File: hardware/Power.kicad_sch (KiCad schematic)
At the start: 5 parts, among them J3 USB_C_Receptacle_USB2.0_16P, U5 USBLC6-2SC6Y

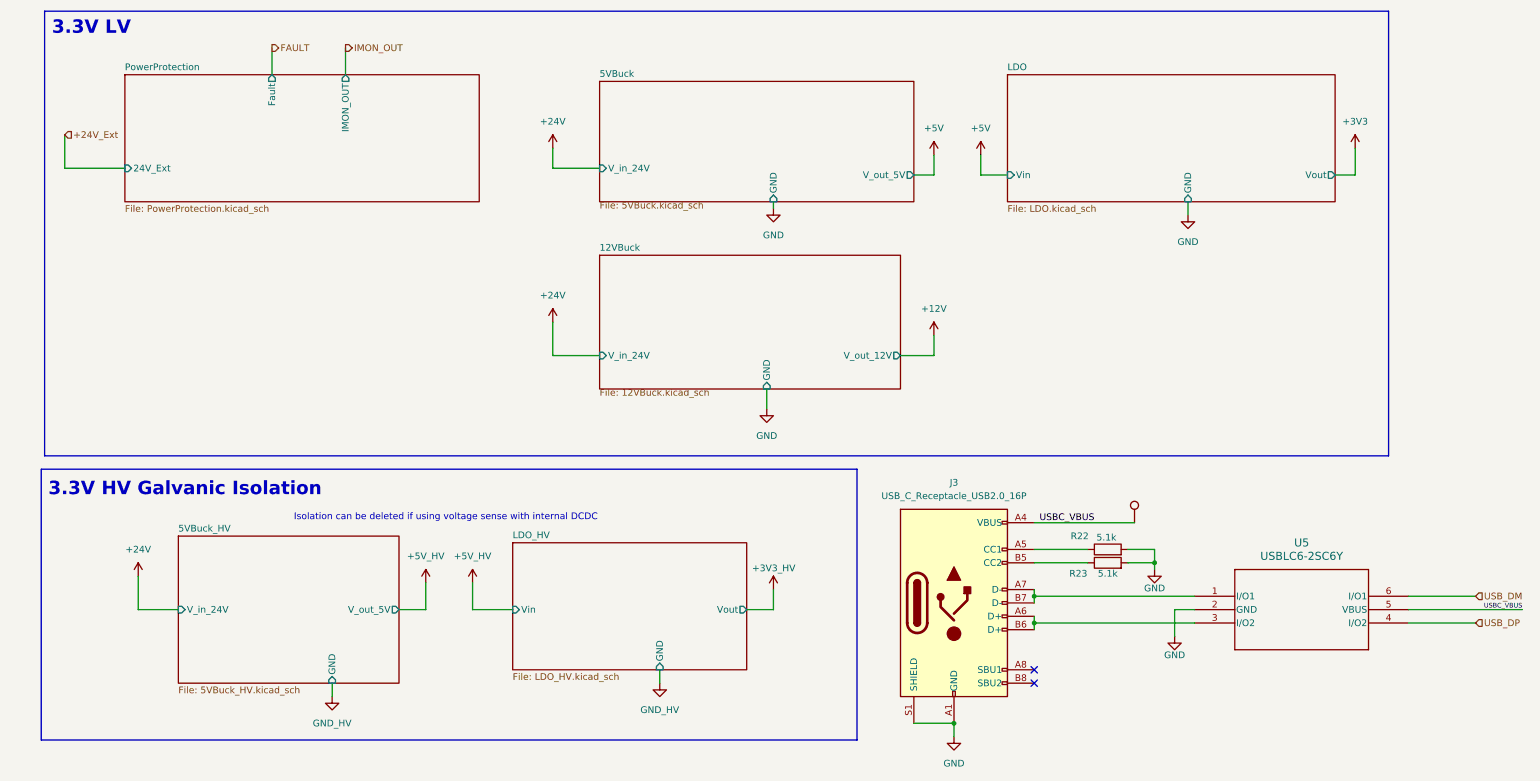
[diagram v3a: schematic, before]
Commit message: addressed 75% of review council 2, cleaned up ERC errors, embedded datasheet and PN
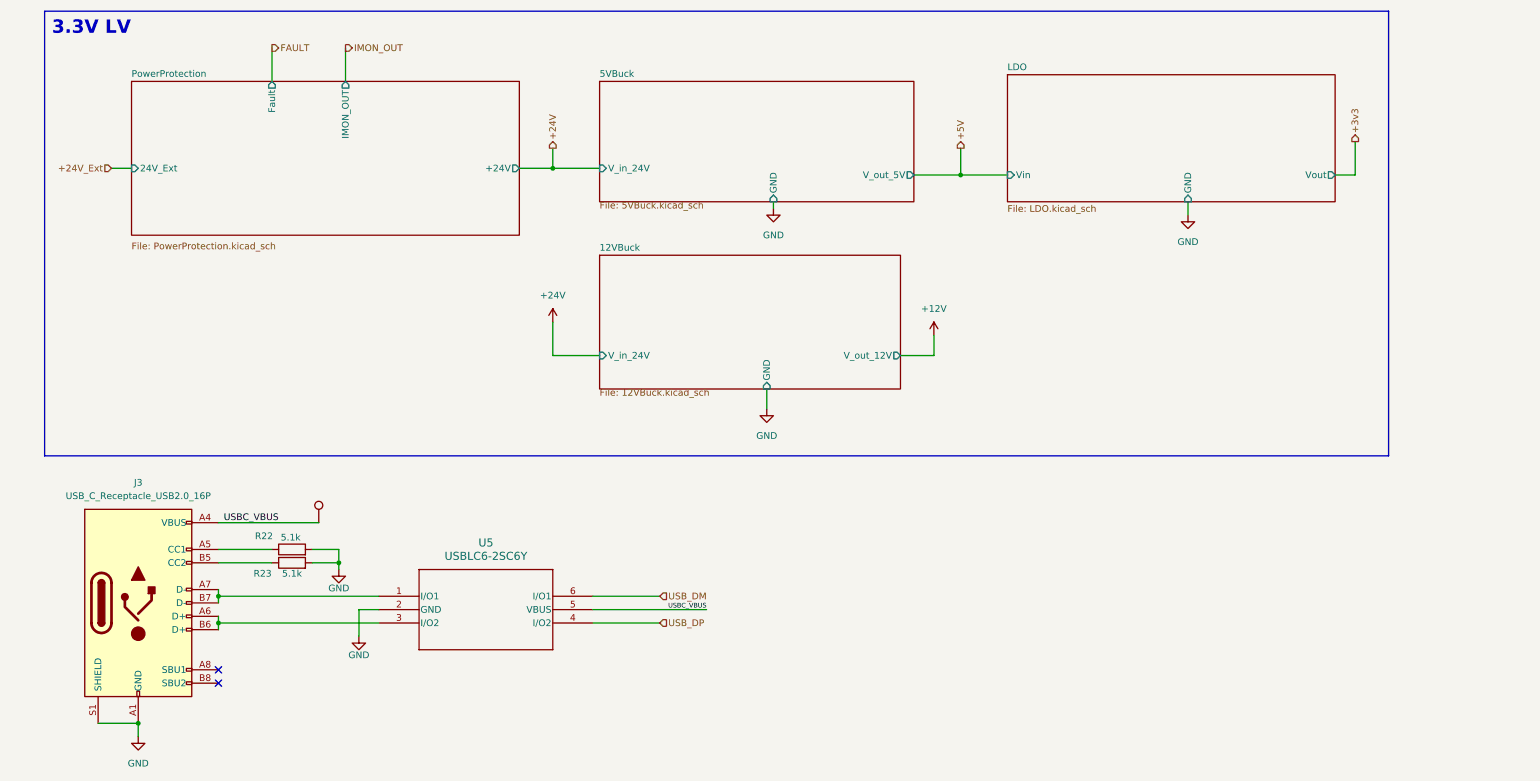
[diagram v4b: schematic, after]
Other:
- removed sheet 5VBuck_HV
- removed sheet LDO_HV
- sheet PowerProtection ports: added +24V; removed none
- note removed: "3.3V HV Galvanic Isolation"
- note removed: "Isolation can be deleted if using voltage sense with internal DCDC"
- moved on the sheet: J3, R22, R23, U5

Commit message: added calcs, cleaned up, addressed comments
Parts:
- added TP12: PP GATE, symbol Connector:TestPoint
- added TP13: PP EN, symbol Connector:TestPoint
- added TP14: PP OV, symbol Connector:TestPoint
- added TP15: PP SOURCE, symbol Connector:TestPoint
- renumbered J3 to J7, R22 to R27, R23 to R28, TP19 to TP11, U5 to U4
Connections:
- new net PowerProtection/EN/UVLO: TP13.1
- new net PowerProtection/OV: TP14.1
- new net PowerProtection/gate: TP12.1
- new net PowerProtection/source: TP15.1
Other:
- removed sheet 12VBuck
- sheet PowerProtection ports: added EN/UVLO, GND, OV, Vin, Vout, gate, source; removed +24V, 24V_Ext, Fault, IMON_OUT
- note added: "Power"
- note removed: "3.3V LV"
- moved on the sheet: J7, R27, R28, U4

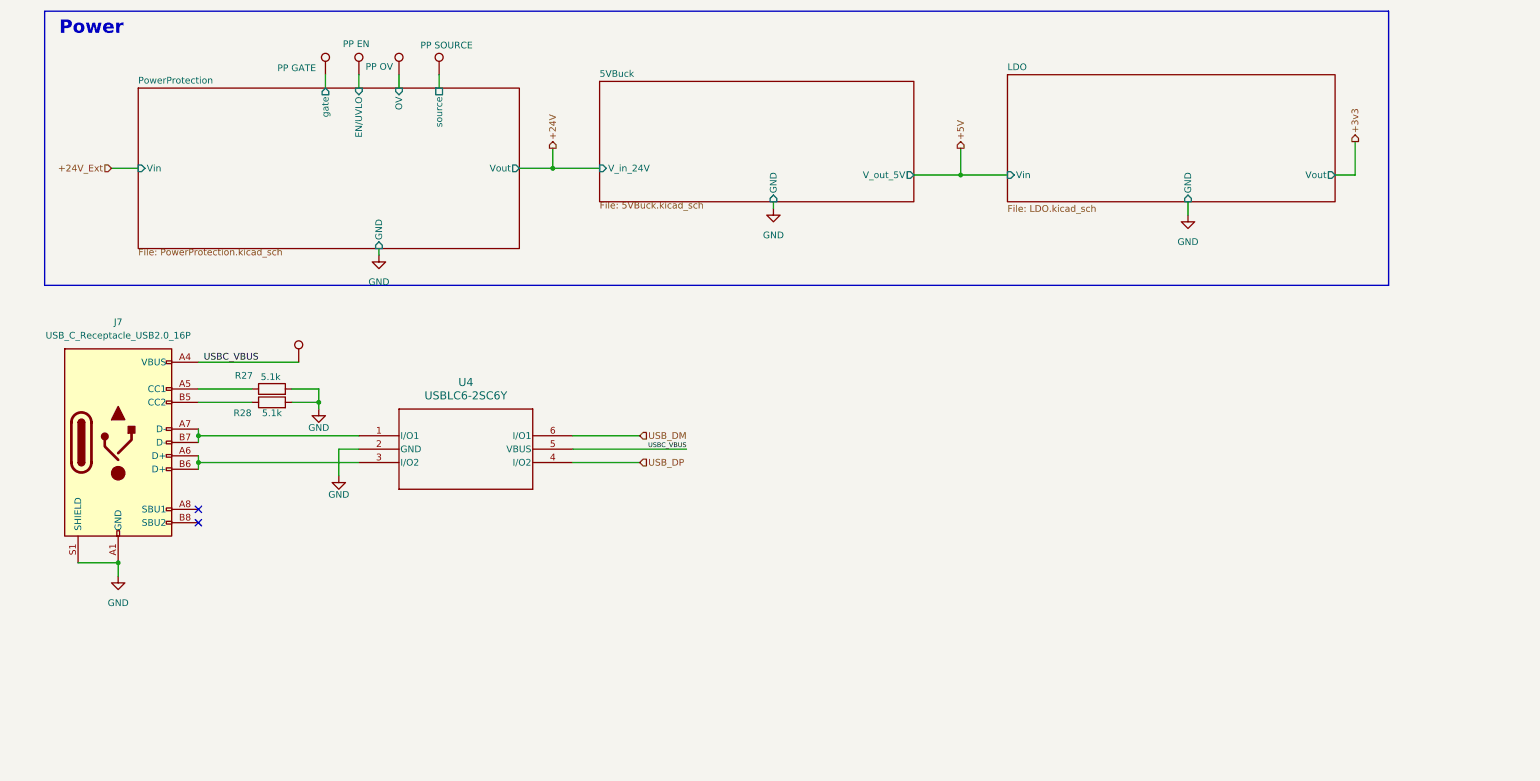
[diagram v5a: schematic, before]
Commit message: added USB power mux
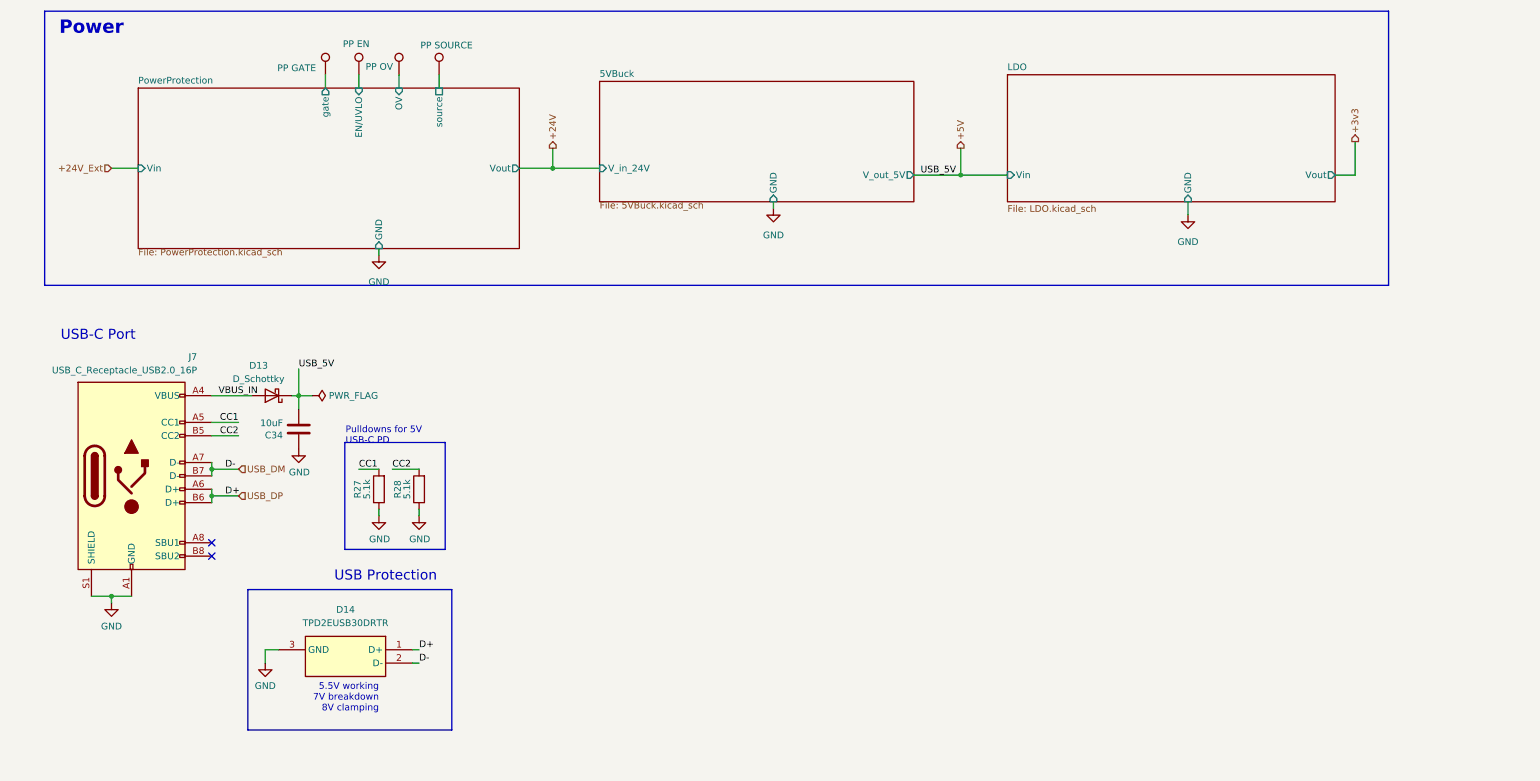
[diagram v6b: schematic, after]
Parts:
- removed J7: USB_C_Receptacle_USB2.0_16P, LHRS_ICs:USB_C_Receptacle_GCT_USB4105-xx-A_16P_TopMnt_Horizontal, symbol lhrs_connectors:USB_C_Receptacle_USB2.0_16P
- removed TP11: TestPoint, symbol Connector:TestPoint
- removed U4: USBLC6-2SC6Y, SOT23-6L_STM, symbol USBLC6_2SC6Y:USBLC6-2SC6Y
- added C34: 10uF, Capacitor_SMD:C_0805_2012Metric, symbol Device:C
- added D13: D_Schottky, Diode_SMD:D_SOD-123, symbol Device:D_Schottky
- added D14: TPD2EUSB30DRTR, UTSVT_ICs:TPD2EUSB30DRTR, symbol USB_PD_Symbols:TPD2EUSB30DRTR
- added J7: USB_C_Receptacle_USB2.0_16P, UTSVT_Connectors:USB_C_Receptacle_GCT_USB4105-xx-A_16P_TopMnt_Horizontal, symbol UTSVT-Connectors:USB_C_Receptacle_USB2.0_16P
- R27, R28: footprint (none) -> Resistor_SMD:R_0603_1608Metric_Pad0.98x0.95mm_HandSolder; LCSC P/N (none) -> C23186; Mouser Part Number (none) -> CRCW06035K10FKEC
- renumbered TP12 to TP11, TP13 to TP12, TP14 to TP13, TP15 to TP14
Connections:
- net +5V: now also C34.2, D13.1 (K)
- net GND: now also R27.1, R28.1, C34.1, D14.3 (GND), J7.A1 (GND), J7.A12 (GND), J7.B1 (GND), J7.B12 (GND), J7.S1 (SHIELD), J7.S2 (Shield), J7.S3 (Shield), J7.S4 (Shield); no longer R27.2, R28.2
- net USB_DM: now also D14.2 (D-), J7.A7 (D-), J7.B7 (D-)
- net USB_DP: now also D14.1 (D+), J7.A6 (D+), J7.B6 (D+)
- new net CC1: J7.A5 (CC1), R27.2
- new net CC2: J7.B5 (CC2), R28.2
- new net VBUS_IN: D13.2 (A), J7.A4 (VBUS), J7.A9 (VBUS), J7.B4 (VBUS), J7.B9 (VBUS)
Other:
- note added: "5.5V working 7V breakdown 8V clamping"
- note added: "Pulldowns for 5V USB-C PD"
- note added: "USB Protection"
- note added: "USB-C Port"

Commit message: fixed ERC warnings
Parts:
- renumbered TP11 to TP12, TP12 to TP13, TP13 to TP14, TP14 to TP15
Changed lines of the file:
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@@
 		(in_pos_files yes)
 		(dnp no)
-		(property "Reference" "TP14"
+		(property "Reference" "TP15"
 			(at 92.456 22.098 0)
 			(hide yes)
@@
 			(project "PS-HVCarrier"
 				(path "/2365a867-6254-4a7c-9718-f325e0bbac5c/904fa10a-747c-46cf-90d1-33d76069dc5d"
-					(reference "TP14")
+					(reference "TP15")
 					(unit 1)
 				)
@@
 		(in_pos_files yes)
 		(dnp no)
-		(property "Reference" "TP13"
+		(property "Reference" "TP14"
 			(at 84.836 22.098 0)
 			(hide yes)
@@
 			(project "PS-HVCarrier"
 				(path "/2365a867-6254-4a7c-9718-f325e0bbac5c/904fa10a-747c-46cf-90d1-33d76069dc5d"
-					(reference "TP13")
+					(reference "TP14")
 					(unit 1)
 				)
@@
 		(dnp no)
 		(fields_autoplaced yes)
-		(property "Reference" "#PWR014"
+		(property "Reference" "#PWR016"
 			(at 82.55 71.12 0)
 			(hide yes)
@@
 			(project "PS-HVCarrier"
 				(path "/2365a867-6254-4a7c-9718-f325e0bbac5c/904fa10a-747c-46cf-90d1-33d76069dc5d"
-					(reference "#PWR014")
+					(reference "#PWR016")
 					(unit 1)
 				)
@@
 		(in_pos_files yes)
 		(dnp no)
-		(property "Reference" "#PWR015"
+		(property "Reference" "#PWR014"
 			(at 60.96 148.59 0)
 			(hide yes)
@@
 			(project "PS-HVCarrier"
 				(path "/2365a867-6254-4a7c-9718-f325e0bbac5c/904fa10a-747c-46cf-90d1-33d76069dc5d"
-					(reference "#PWR015")
+					(reference "#PWR014")
 					(unit 1)
 				)
@@
 		(in_pos_files yes)
 		(dnp no)
-		(property "Reference" "TP11"
+		(property "Reference" "TP12"
 			(at 70.358 21.844 0)
 			(hide yes)
@@
 			(project "PS-HVCarrier"
 				(path "/2365a867-6254-4a7c-9718-f325e0bbac5c/904fa10a-747c-46cf-90d1-33d76069dc5d"
-					(reference "TP11")
+					(reference "TP12")
 					(unit 1)
 				)
@@
 		(in_pos_files yes)
 		(dnp no)
-		(property "Reference" "#PWR016"
+		(property "Reference" "#PWR015"
 			(at 67.31 107.95 0)
 			(hide yes)
@@
 			(project "PS-HVCarrier"
 				(path "/2365a867-6254-4a7c-9718-f325e0bbac5c/904fa10a-747c-46cf-90d1-33d76069dc5d"
-					(reference "#PWR016")
+					(reference "#PWR015")
 					(unit 1)
 				)
@@
 		(in_pos_files yes)
 		(dnp no)
-		(property "Reference" "TP12"
+		(property "Reference" "TP13"
 			(at 77.216 22.098 0)
 			(hide yes)
@@
 			(project "PS-HVCarrier"
 				(path "/2365a867-6254-4a7c-9718-f325e0bbac5c/904fa10a-747c-46cf-90d1-33d76069dc5d"
-					(reference "TP12")
-					(unit 1)
-				)
+					(reference "TP13")
+					(unit 1)
+				)

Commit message: added pin layout ss, resolved erc errors, added p/n
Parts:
- D14: footprint UTSVT_ICs:TPD2EUSB30DRTR -> LHRS_ICs:TPD2EUSB30DRTR
- J7: footprint UTSVT_Connectors:USB_C_Receptacle_GCT_USB4105-xx-A_16P_TopMnt_Horizontal -> LHRS_Connectors:USB_C_Receptacle_GCT_USB4105-xx-A_16P_TopMnt_Horizontal
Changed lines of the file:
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@@
 	)
 	(rectangle
-		(start 96.393 128.27)
-		(end 57.658 154.94)
+		(start 57.658 128.27)
+		(end 101.346 154.94)
 		(stroke
 			(width 0)
@@
 		)
 	)
-	(label "D+"
-		(at 90.17 139.7 0)
-		(effects
-			(font
-				(size 1.27 1.27)
-			)
-			(justify left bottom)
-		)
-	)
 	(label "CC1"
 		(at 78.74 105.41 0)
@@
 		)
 	)
-	(label "USB_5V"
-		(at 67.31 86.36 0)
-		(effects
-			(font
-				(size 1.27 1.27)
-			)
-			(justify left bottom)
-		)
-	)
-	(label "D-"
-		(at 53.34 105.41 0)
-		(effects
-			(font
-				(size 1.27 1.27)
-			)
-			(justify left bottom)
-		)
-	)
-	(label "D+"
-		(at 53.34 110.49 0)
-		(effects
-			(font
-				(size 1.27 1.27)
-			)
-			(justify left bottom)
-		)
-	)
 	(label "CC1"
 		(at 55.88 96.52 180)
@@
 	(label "CC2"
 		(at 85.09 105.41 0)
-		(effects
-			(font
-				(size 1.27 1.27)
-			)
-			(justify left bottom)
-		)
-	)
-	(label "D-"
-		(at 90.17 142.24 0)
-		(effects
-			(font
-				(size 1.27 1.27)
-			)
-			(justify left bottom)
-		)
-	)
-	(label "USB_5V"
-		(at 185.42 49.53 0)
 		(effects
 			(font
@@
 		)
 	)
+	(hierarchical_label "+5V"
+		(shape output)
+		(at 67.31 86.36 90)
+		(effects
+			(font
+				(size 1.27 1.27)
+			)
+			(justify left)
+		)
+	)
+	(hierarchical_label "USB_DP"
+		(shape input)
+		(at 90.17 139.7 0)
+		(effects
+			(font
+				(size 1.27 1.27)
+			)
+			(justify left)
+		)
+	)
 	(hierarchical_label "+24V"
 		(shape output)
 		(at 115.57 44.45 90)
+		(effects
+			(font
+				(size 1.27 1.27)
+			)
+			(justify left)
+		)
+	)
+	(hierarchical_label "USB_DM"
+		(shape input)
+		(at 90.17 142.24 0)
 		(effects
 			(font
@@
 			)
 		)
-		(property "Footprint" "UTSVT_ICs:TPD2EUSB30DRTR"
+		(property "Footprint" "LHRS_ICs:TPD2EUSB30DRTR"
 			(at 67.31 234.62 0)
 			(hide yes)
@@
 			)
 		)
-		(property "Footprint" "UTSVT_Connectors:USB_C_Receptacle_GCT_USB4105-xx-A_16P_TopMnt_Horizontal"
+		(property "Footprint" "LHRS_Connectors:USB_C_Receptacle_GCT_USB4105-xx-A_16P_TopMnt_Horizontal"
 			(at 39.37 106.68 0)
 			(hide yes)
